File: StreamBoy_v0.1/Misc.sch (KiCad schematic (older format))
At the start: 3 parts, among them IC1 LY68L6400SLIT, J2 USB_B_Micro, U4 CP2102N-A01-GQFN24

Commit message: Bunch of stuff
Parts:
- added C10, C5, C6, C7, C8, C9, C? (x2): C, Capacitor_SMD:C_0805_2012Metric, symbol Device:C
- added J?: TF-015, TF015, symbol TF-015:TF-015
- added Q1, Q2: SS8050-G, SOT95P240X115-3N, symbol SS8050-G:SS8050-G
- added R47, R48, R49, R50, R51: R, Resistor_SMD:R_0805_2012Metric, symbol Device:R
- added X?: SG-7050CBN, Oscillator:Oscillator_SMD_SeikoEpson_SG8002CA-4Pin_7.0x5.0mm, symbol Oscillator:SG-7050CBN
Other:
- moved on the sheet: IC1

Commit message: Power to the masses
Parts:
- removed C?: C, Capacitor_SMD:C_0805_2012Metric, symbol Device:C
- added C2: 15pF, Capacitor_SMD:C_0805_2012Metric, symbol Device:C
- C1: renamed from C?; value C -> 0.1uF
- gave numbers to parts that had none: 1
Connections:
- net labels added: FPGA_CLK_50M, GND, USB5V
- wire segments 8 -> 14
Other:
- moved on the sheet: C1, X1
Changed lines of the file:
@@
 $EndComp
 $Comp
-L Oscillator:SG-7050CBN X?
+L Oscillator:SG-7050CBN X1
 U 1 1 5E0DA99D
-P 8150 4850
-F 0 "X?" H 8494 4896 50  0000 L CNN
-F 1 "SG-7050CBN" H 8494 4805 50  0000 L CNN
-F 2 "Oscillator:Oscillator_SMD_SeikoEpson_SG8002CA-4Pin_7.0x5.0mm" H 8850 4500 50  0001 C CNN
-F 3 "https://support.epson.biz/td/api/doc_check.php?dl=brief_SG7050CBN&lang=en" H 8050 4850 50  0001 C CNN
-	1    8150 4850
+P 9850 5750
+F 0 "X1" H 10000 5500 50  0000 L CNN
+F 1 "SG-7050CBN" H 10000 5400 50  0000 L CNN
+F 2 "Oscillator:Oscillator_SMD_SeikoEpson_SG8002CA-4Pin_7.0x5.0mm" H 10550 5400 50  0001 C CNN
+F 3 "https://support.epson.biz/td/api/doc_check.php?dl=brief_SG7050CBN&lang=en" H 9750 5750 50  0001 C CNN
+	1    9850 5750
 	1    0    0    -1
 $EndComp
@@
 L Device:C C?
 U 1 1 5E0DB62B
-P 9450 4900
+P 9850 5150
 AR Path="/5E0FF68C/5E0DB62B" Ref="C?"  Part="1"
-AR Path="/5E07E0B7/5E0DB62B" Ref="C?"  Part="1"
-F 0 "C?" H 9565 4946 50  0000 L CNN
-F 1 "C" H 9565 4855 50  0000 L CNN
-F 2 "Capacitor_SMD:C_0805_2012Metric" H 9488 4750 50  0001 C CNN
-F 3 "~" H 9450 4900 50  0001 C CNN
-	1    9450 4900
+AR Path="/5E07E0B7/5E0DB62B" Ref="C1"  Part="1"
+F 0 "C1" H 9965 5196 50  0000 L CNN
+F 1 "0.1uF" H 9965 5105 50  0000 L CNN
+F 2 "Capacitor_SMD:C_0805_2012Metric" H 9888 5000 50  0001 C CNN
+F 3 "https://datasheet.lcsc.com/szlcsc/1912111437_Shenzhen-SCTF-Elec-S7D50-000000A20F30T_C387131.pdf" H 9850 5150 50  0001 C CNN
+	1    9850 5150
 	1    0    0    -1
 $EndComp
 $Comp
 L Device:C C?
-U 1 1 5E0DB631
-P 9800 4900
-AR Path="/5E0FF68C/5E0DB631" Ref="C?"  Part="1"
-AR Path="/5E07E0B7/5E0DB631" Ref="C?"  Part="1"
-F 0 "C?" H 9915 4946 50  0000 L CNN
-F 1 "C" H 9915 4855 50  0000 L CNN
-F 2 "Capacitor_SMD:C_0805_2012Metric" H 9838 4750 50  0001 C CNN
-F 3 "~" H 9800 4900 50  0001 C CNN
-	1    9800 4900
+U 1 1 5E0F5C50
+P 10450 5750
+AR Path="/5E0FF68C/5E0F5C50" Ref="C?"  Part="1"
+AR Path="/5E07E0B7/5E0F5C50" Ref="C2"  Part="1"
+F 0 "C2" H 10565 5796 50  0000 L CNN
+F 1 "15pF" H 10565 5705 50  0000 L CNN
+F 2 "Capacitor_SMD:C_0805_2012Metric" H 10488 5600 50  0001 C CNN
+F 3 "https://datasheet.lcsc.com/szlcsc/1912111437_Shenzhen-SCTF-Elec-S7D50-000000A20F30T_C387131.pdf" H 10450 5750 50  0001 C CNN
+	1    10450 5750
+	0    -1   -1   0
+$EndComp
+Text GLabel 9850 5000 1    50   Input ~ 0
+VCC3
+Wire Wire Line
+	10150 5750 10300 5750
+Wire Wire Line
+	10300 5750 10300 5450
+Connection ~ 10300 5750
+Text GLabel 10300 5450 1    50   Input ~ 0
+FPGA_CLK_50M
+$Comp
+L power:GND #PWR?
+U 1 1 5E0FED92
+P 10600 5750
+F 0 "#PWR?" H 10600 5500 50  0001 C CNN
+F 1 "GND" V 10605 5622 50  0000 R CNN
+F 2 "" H 10600 5750 50  0001 C CNN
+F 3 "" H 10600 5750 50  0001 C CNN
+	1    10600 5750
+	0    -1   -1   0
+$EndComp
+Wire Wire Line
+	9850 5300 9850 5450
+Wire Wire Line
+	9850 5450 9550 5450
+Wire Wire Line
+	9550 5450 9550 5750
+Connection ~ 9850 5450
+$Comp
+L power:GND #PWR?
+U 1 1 5E100DF1
+P 9850 6050
+F 0 "#PWR?" H 9850 5800 50  0001 C CNN
+F 1 "GND" H 9855 5877 50  0000 C CNN
+F 2 "" H 9850 6050 50  0001 C CNN
+F 3 "" H 9850 6050 50  0001 C CNN
+	1    9850 6050
 	1    0    0    -1
 $EndComp
+Wire Wire Line
+	3250 4300 3100 4300
+Text GLabel 3250 4300 2    50   Input ~ 0
+USB5V
 $EndSCHEMATC

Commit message: Connect uart
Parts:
- removed C10, C5, C6, C7, C8, C9: C, Capacitor_SMD:C_0805_2012Metric, symbol Device:C
- removed J?: TF-015, TF015, symbol TF-015:TF-015
- removed Q1, Q2: SS8050-G, SOT95P240X115-3N, symbol SS8050-G:SS8050-G
- removed R47, R48, R49, R50, R51: R, Resistor_SMD:R_0805_2012Metric, symbol Device:R
- removed U4: CP2102N-A01-GQFN24, Package_DFN_QFN:QFN-24-1EP_4x4mm_P0.5mm_EP2.6x2.6mm, symbol Interface_USB:CP2102N-A01-GQFN24
- added C? (x2): 0.1uF, Capacitor_SMD:C_0805_2012Metric, symbol Device:C
- added C?: 1uF, Capacitor_SMD:C_0805_2012Metric, symbol Device:C
- added C?: 4.7uF, Capacitor_SMD:C_0805_2012Metric, symbol Device:C
- added Q? (x2): SS8050-G, SOT95P240X115-3N, symbol SS8050-G:SS8050-G
- added R? (x3): 10K, Resistor_SMD:R_0805_2012Metric, symbol Device:R
- added R?: 2K, Resistor_SMD:R_0805_2012Metric, symbol Device:R
- added UUART: CP2102N-A01-GQFN28, Package_DFN_QFN:QFN-28-1EP_5x5mm_P0.5mm_EP3.35x3.35mm, symbol Interface_USB:CP2102N-A01-GQFN28
- renumbered J2 to JUSB
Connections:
- net labels added: ESP_DTR, ESP_EN, ESP_IO0, ESP_RTS, ESP_RX, ESP_TX
- wire segments 14 -> 59
- no-connect marks 0 -> 16
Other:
- moved on the sheet: IC1, JUSB

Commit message: Flip RX/TX, Move esp prog. circuit
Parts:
- removed Q? (x2): SS8050-G, SOT95P240X115-3N, symbol SS8050-G:SS8050-G
- removed R? (x2): 10K, Resistor_SMD:R_0805_2012Metric, symbol Device:R
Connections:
- net labels removed: ESP_EN, ESP_IO0
- wire segments 59 -> 45
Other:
- note added: "Note, RX/TX are flipped"
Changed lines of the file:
@@
 	0    -1   -1   0
-$EndComp
-$Comp
-L Device:R R?
-U 1 1 5E0BF601
-P 8700 1650
-AR Path="/5E0FF68C/5E0BF601" Ref="R?"  Part="1"
-AR Path="/5E07E0B7/5E0BF601" Ref="R?"  Part="1"
-F 0 "R?" H 8770 1696 50  0000 L CNN
-F 1 "10K" H 8770 1605 50  0000 L CNN
-F 2 "Resistor_SMD:R_0805_2012Metric" V 8630 1650 50  0001 C CNN
-F 3 "~" H 8700 1650 50  0001 C CNN
-	1    8700 1650
-	0    1    1    0
-$EndComp
-$Comp
-L Device:R R?
-U 1 1 5E0BFA7F
-P 8700 2400
-AR Path="/5E0FF68C/5E0BFA7F" Ref="R?"  Part="1"
-AR Path="/5E07E0B7/5E0BFA7F" Ref="R?"  Part="1"
-F 0 "R?" H 8770 2446 50  0000 L CNN
-F 1 "10K" H 8770 2355 50  0000 L CNN
-F 2 "Resistor_SMD:R_0805_2012Metric" V 8630 2400 50  0001 C CNN
-F 3 "~" H 8700 2400 50  0001 C CNN
-	1    8700 2400
-	0    1    1    0
-$EndComp
-$Comp
-L SS8050-G:SS8050-G Q?
-U 1 1 5E0BFFFE
-P 9100 1650
-F 0 "Q?" H 9638 1696 50  0000 L CNN
-F 1 "SS8050-G" H 9638 1605 50  0000 L CNN
-F 2 "SOT95P240X115-3N" H 9100 1650 50  0001 L BNN
-F 3 "1.15mm" H 9100 1650 50  0001 L BNN
-F 4 "Bipolar Transistors - BJT NPN TRANSISTOR 1.5A 40V" H 9100 1650 50  0001 L BNN "Field4"
-F 5 "Comchip Technology" H 9100 1650 50  0001 L BNN "Field5"
-F 6 "" H 9100 1650 50  0001 L BNN "Field6"
-F 7 "" H 9100 1650 50  0001 L BNN "Field7"
-F 8 "SS8050-G" H 9100 1650 50  0001 L BNN "Field8"
-	1    9100 1650
-	1    0    0    -1
-$EndComp
-$Comp
-L SS8050-G:SS8050-G Q?
-U 1 1 5E0C0B15
-P 9100 2400
-F 0 "Q?" H 9638 2446 50  0000 L CNN
-F 1 "SS8050-G" H 9638 2355 50  0000 L CNN
-F 2 "SOT95P240X115-3N" H 9100 2400 50  0001 L BNN
-F 3 "1.15mm" H 9100 2400 50  0001 L BNN
-F 4 "Bipolar Transistors - BJT NPN TRANSISTOR 1.5A 40V" H 9100 2400 50  0001 L BNN "Field4"
-F 5 "Comchip Technology" H 9100 2400 50  0001 L BNN "Field5"
-F 6 "" H 9100 2400 50  0001 L BNN "Field6"
-F 7 "" H 9100 2400 50  0001 L BNN "Field7"
-F 8 "SS8050-G" H 9100 2400 50  0001 L BNN "Field8"
-	1    9100 2400
-	1    0    0    1
 $EndComp
 Text GLabel 3800 1850 2    50   Input ~ 0
 ESP_RTS
+Text GLabel 3800 2050 2    50   Input ~ 0
+ESP_RX
 Text GLabel 3800 1950 2    50   Input ~ 0
-ESP_RX
-Text GLabel 3800 2050 2    50   Input ~ 0
 ESP_TX
 Text GLabel 3800 2250 2    50   Input ~ 0
 ESP_DTR
-Text GLabel 8250 1650 0    50   Input ~ 0
-ESP_DTR
-Text GLabel 8250 2400 0    50   Input ~ 0
-ESP_RTS
-Wire Wire Line
-	8250 1650 8450 1650
-Wire Wire Line
-	8550 2400 8500 2400
-Wire Wire Line
-	9100 2400 8850 2400
-Wire Wire Line
-	8850 1650 9100 1650
-Text GLabel 10300 1250 2    50   Input ~ 0
-ESP_EN
-Text GLabel 10300 2800 2    50   Input ~ 0
-ESP_IO0
-Wire Wire Line
-	10300 1250 9500 1250
-Wire Wire Line
-	9500 1250 9500 1350
-Wire Wire Line
-	10300 2800 9500 2800
-Wire Wire Line
-	9500 2800 9500 2700
-Wire Wire Line
-	9500 1950 8500 1950
-Wire Wire Line
-	8500 1950 8500 2400
-Connection ~ 8500 2400
-Wire Wire Line
-	8500 2400 8250 2400
-Wire Wire Line
-	9500 2100 8450 2100
-Wire Wire Line
-	8450 2100 8450 1650
-Connection ~ 8450 1650
-Wire Wire Line
-	8450 1650 8550 1650
 Text GLabel 2100 1950 0    50   Input ~ 0
 VCC3
@@
 Wire Wire Line
 	1950 2350 2650 2350
+Text Notes 4150 2000 0    50   ~ 0
+Note, RX/TX are flipped
 $EndSCHEMATC

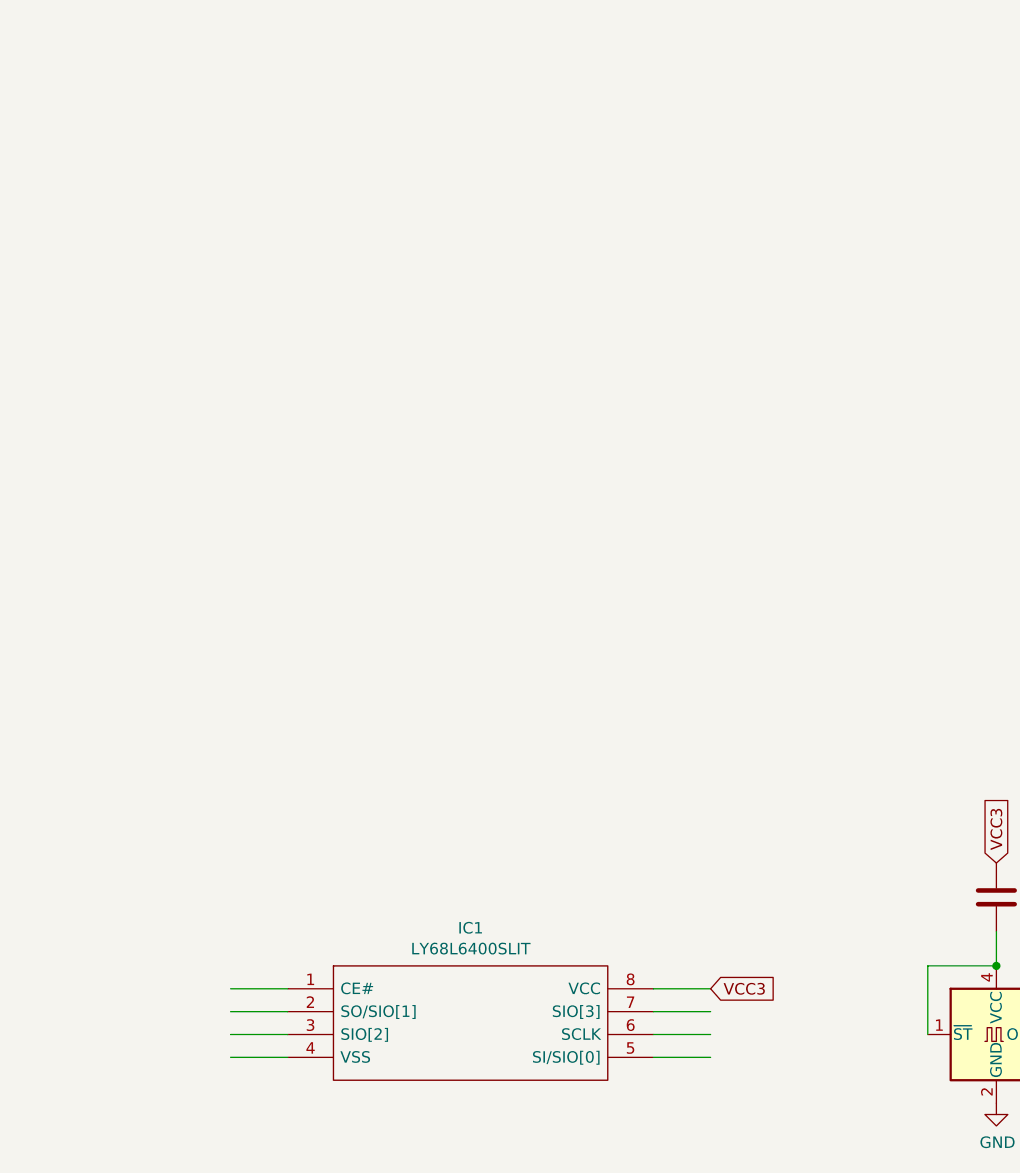
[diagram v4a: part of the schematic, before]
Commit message: Connect RAM temporarily
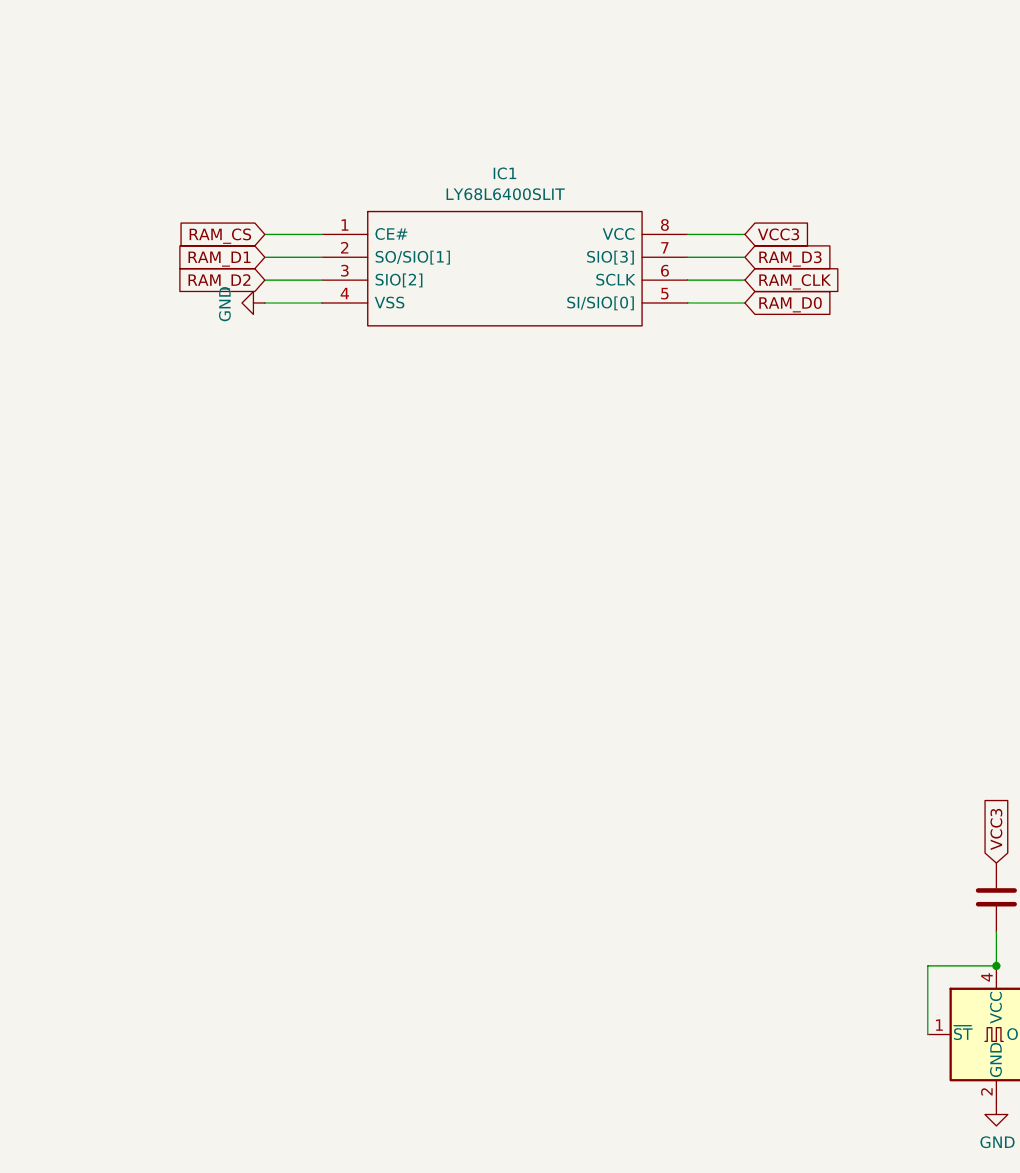
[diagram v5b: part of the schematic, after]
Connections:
- net labels added: RAM_CLK, RAM_CS, RAM_D0, RAM_D1, RAM_D2, RAM_D3
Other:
- moved on the sheet: IC1
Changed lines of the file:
@@
 $EndDescr
-$Comp
-L LY68L6400SLIT:LY68L6400SLIT IC1
-U 1 1 5E092BFD
-P 6750 5550
-F 0 "IC1" H 7550 5815 50  0000 C CNN
-F 1 "LY68L6400SLIT" H 7550 5724 50  0000 C CNN
-F 2 "SOIC127P600X175-8N" H 8200 5650 50  0001 L CNN
-F 3 "https://datasheet.lcsc.com/szlcsc/Lyontek-Inc-LY68L6400SLIT_C261881.pdf" H 8200 5550 50  0001 L CNN
-F 4 "AM SRAM 64Mb (8M x 8) SPI/ QPI SOP-8_150mil RoHS" H 8200 5450 50  0001 L CNN "Description"
-F 5 "1.75" H 8200 5350 50  0001 L CNN "Height"
-F 6 "Lyontek Inc." H 8200 5250 50  0001 L CNN "Manufacturer_Name"
-F 7 "LY68L6400SLIT" H 8200 5150 50  0001 L CNN "Manufacturer_Part_Number"
-F 8 "" H 8200 5050 50  0001 L CNN "Mouser Part Number"
-F 9 "" H 8200 4950 50  0001 L CNN "Mouser Price/Stock"
-F 10 "" H 8200 4850 50  0001 L CNN "RS Part Number"
-F 11 "" H 8200 4750 50  0001 L CNN "RS Price/Stock"
-	1    6750 5550
-	1    0    0    -1
-$EndComp
-Wire Wire Line
-	6750 5550 6500 5550
-Wire Wire Line
-	6750 5650 6500 5650
-Wire Wire Line
-	6750 5750 6500 5750
-Wire Wire Line
-	6750 5850 6500 5850
-Wire Wire Line
-	8350 5850 8600 5850
-Wire Wire Line
-	8350 5750 8600 5750
-Wire Wire Line
-	8350 5650 8600 5650
-Wire Wire Line
-	8350 5550 8600 5550
-Text GLabel 8600 5550 2    50   Input ~ 0
-VCC3
 $Comp
 L Oscillator:SG-7050CBN X1
@@
 Text Notes 4150 2000 0    50   ~ 0
 Note, RX/TX are flipped
+Text GLabel 8750 2250 2    50   Input ~ 0
+VCC3
+Wire Wire Line
+	8500 2250 8750 2250
+Wire Wire Line
+	8500 2350 8750 2350
+Wire Wire Line
+	8500 2450 8750 2450
+Wire Wire Line
+	8500 2550 8750 2550
+Wire Wire Line
+	6900 2550 6650 2550
+Wire Wire Line
+	6900 2450 6650 2450
+Wire Wire Line
+	6900 2350 6650 2350
+Wire Wire Line
+	6900 2250 6650 2250
+$Comp
+L LY68L6400SLIT:LY68L6400SLIT IC1
+U 1 1 5E092BFD
+P 6900 2250
+F 0 "IC1" H 7700 2515 50  0000 C CNN
+F 1 "LY68L6400SLIT" H 7700 2424 50  0000 C CNN
+F 2 "SOIC127P600X175-8N" H 8350 2350 50  0001 L CNN
+F 3 "https://datasheet.lcsc.com/szlcsc/Lyontek-Inc-LY68L6400SLIT_C261881.pdf" H 8350 2250 50  0001 L CNN
+F 4 "AM SRAM 64Mb (8M x 8) SPI/ QPI SOP-8_150mil RoHS" H 8350 2150 50  0001 L CNN "Description"
+F 5 "1.75" H 8350 2050 50  0001 L CNN "Height"
+F 6 "Lyontek Inc." H 8350 1950 50  0001 L CNN "Manufacturer_Name"
+F 7 "LY68L6400SLIT" H 8350 1850 50  0001 L CNN "Manufacturer_Part_Number"
+F 8 "" H 8350 1750 50  0001 L CNN "Mouser Part Number"
+F 9 "" H 8350 1650 50  0001 L CNN "Mouser Price/Stock"
+F 10 "" H 8350 1550 50  0001 L CNN "RS Part Number"
+F 11 "" H 8350 1450 50  0001 L CNN "RS Price/Stock"
+	1    6900 2250
+	1    0    0    -1
+$EndComp
+Text GLabel 8750 2450 2    50   Input ~ 0
+RAM_CLK
+Text GLabel 8750 2550 2    50   Input ~ 0
+RAM_D0
+Text GLabel 8750 2350 2    50   Input ~ 0
+RAM_D3
+Text GLabel 6650 2450 0    50   Input ~ 0
+RAM_D2
+Text GLabel 6650 2350 0    50   Input ~ 0
+RAM_D1
+Text GLabel 6650 2250 0    50   Input ~ 0
+RAM_CS
+$Comp
+L power:GND #PWR?
+U 1 1 5E179831
+P 6650 2550
+F 0 "#PWR?" H 6650 2300 50  0001 C CNN
+F 1 "GND" H 6655 2377 50  0000 C CNN
+F 2 "" H 6650 2550 50  0001 C CNN
+F 3 "" H 6650 2550 50  0001 C CNN
+	1    6650 2550
+	0    1    1    0
+$EndComp
 $EndSCHEMATC

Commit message: Update some labels
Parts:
- gave numbers to parts that had none: 6
- renumbered JUSB to JUSB1, UUART to U12
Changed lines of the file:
@@
 $EndComp
 $Comp
-L power:GND #PWR?
+L power:GND #PWR0125
 U 1 1 5E0AE37F
 P 1000 2900
-F 0 "#PWR?" H 1000 2650 50  0001 C CNN
+F 0 "#PWR0125" H 1000 2650 50  0001 C CNN
 F 1 "GND" H 1005 2727 50  0000 C CNN
 F 2 "" H 1000 2900 50  0001 C CNN
@@
 P 3900 2650
 AR Path="/5E0FF68C/5E0B4B8D" Ref="R?"  Part="1"
-AR Path="/5E07E0B7/5E0B4B8D" Ref="R?"  Part="1"
-F 0 "R?" H 3970 2696 50  0000 L CNN
+AR Path="/5E07E0B7/5E0B4B8D" Ref="R12"  Part="1"
+F 0 "R12" H 3970 2696 50  0000 L CNN
 F 1 "10K" H 3970 2605 50  0000 L CNN
 F 2 "Resistor_SMD:R_0805_2012Metric" V 3830 2650 50  0001 C CNN
@@
 $EndComp
 $Comp
-L power:GND #PWR?
+L power:GND #PWR0126
 U 1 1 5E0B51BC
 P 4200 2650
-F 0 "#PWR?" H 4200 2400 50  0001 C CNN
+F 0 "#PWR0126" H 4200 2400 50  0001 C CNN
 F 1 "GND" H 4205 2477 50  0000 C CNN
 F 2 "" H 4200 2650 50  0001 C CNN
@@
 P 2400 1950
 AR Path="/5E0FF68C/5E0D0203" Ref="R?"  Part="1"
-AR Path="/5E07E0B7/5E0D0203" Ref="R?"  Part="1"
-F 0 "R?" H 2470 1996 50  0000 L CNN
+AR Path="/5E07E0B7/5E0D0203" Ref="R11"  Part="1"
+F 0 "R11" H 2470 1996 50  0000 L CNN
 F 1 "2K" H 2470 1905 50  0000 L CNN
 F 2 "Resistor_SMD:R_0805_2012Metric" V 2330 1950 50  0001 C CNN
@@
 P 2700 1200
 AR Path="/5E0FF68C/5E0DC6A6" Ref="C?"  Part="1"
-AR Path="/5E07E0B7/5E0DC6A6" Ref="C?"  Part="1"
-F 0 "C?" H 2815 1246 50  0000 L CNN
+AR Path="/5E07E0B7/5E0DC6A6" Ref="C8"  Part="1"
+F 0 "C8" H 2815 1246 50  0000 L CNN
 F 1 "0.1uF" H 2815 1155 50  0000 L CNN
 F 2 "Capacitor_SMD:C_0805_2012Metric" H 2738 1050 50  0001 C CNN
@@
 P 2200 1200
 AR Path="/5E0FF68C/5E0DDFA3" Ref="C?"  Part="1"
-AR Path="/5E07E0B7/5E0DDFA3" Ref="C?"  Part="1"
-F 0 "C?" H 2315 1246 50  0000 L CNN
+AR Path="/5E07E0B7/5E0DDFA3" Ref="C7"  Part="1"
+F 0 "C7" H 2315 1246 50  0000 L CNN
 F 1 "1uF" H 2315 1155 50  0000 L CNN
 F 2 "Capacitor_SMD:C_0805_2012Metric" H 2238 1050 50  0001 C CNN
@@
 $EndComp
 $Comp
-L power:GND #PWR?
+L power:GND #PWR0127
 U 1 1 5E0DE66B
 P 2200 900
-F 0 "#PWR?" H 2200 650 50  0001 C CNN
+F 0 "#PWR0127" H 2200 650 50  0001 C CNN
 F 1 "GND" H 2205 727 50  0000 C CNN
 F 2 "" H 2200 900 50  0001 C CNN
@@
 VCC3
 $Comp
-L Interface_USB:CP2102N-A01-GQFN28 UUART
+L Interface_USB:CP2102N-A01-GQFN28 U12
 U 1 1 5E0E977D
 P 3150 2850
-F 0 "UUART" H 3150 1461 50  0000 C CNN
+F 0 "U12" H 3150 1461 50  0000 C CNN
 F 1 "CP2102N-A01-GQFN28" H 3150 1370 50  0000 C CNN
 F 2 "Package_DFN_QFN:QFN-28-1EP_5x5mm_P0.5mm_EP3.35x3.35mm" H 3600 1650 50  0001 L CNN
@@
 P 4000 1200
 AR Path="/5E0FF68C/5E102D99" Ref="C?"  Part="1"
-AR Path="/5E07E0B7/5E102D99" Ref="C?"  Part="1"
-F 0 "C?" H 4115 1246 50  0000 L CNN
+AR Path="/5E07E0B7/5E102D99" Ref="C10"  Part="1"
+F 0 "C10" H 4115 1246 50  0000 L CNN
 F 1 "0.1uF" H 4115 1155 50  0000 L CNN
 F 2 "Capacitor_SMD:C_0805_2012Metric" H 4038 1050 50  0001 C CNN
@@
 P 3500 1200
 AR Path="/5E0FF68C/5E102D9F" Ref="C?"  Part="1"
-AR Path="/5E07E0B7/5E102D9F" Ref="C?"  Part="1"
-F 0 "C?" H 3615 1246 50  0000 L CNN
+AR Path="/5E07E0B7/5E102D9F" Ref="C9"  Part="1"
+F 0 "C9" H 3615 1246 50  0000 L CNN
 F 1 "4.7uF" H 3615 1155 50  0000 L CNN
 F 2 "Capacitor_SMD:C_0805_2012Metric" H 3538 1050 50  0001 C CNN
@@
 $EndComp
 $Comp
-L power:GND #PWR?
+L power:GND #PWR0128
 U 1 1 5E102DA5
 P 3500 900
-F 0 "#PWR?" H 3500 650 50  0001 C CNN
+F 0 "#PWR0128" H 3500 650 50  0001 C CNN
 F 1 "GND" H 3505 727 50  0000 C CNN
 F 2 "" H 3500 900 50  0001 C CNN
@@
 NoConn ~ 3650 3950
 $Comp
-L power:GND #PWR?
+L power:GND #PWR0129
 U 1 1 5E12E83F
 P 3150 4400
-F 0 "#PWR?" H 3150 4150 50  0001 C CNN
+F 0 "#PWR0129" H 3150 4150 50  0001 C CNN
 F 1 "GND" H 3155 4227 50  0000 C CNN
 F 2 "" H 3150 4400 50  0001 C CNN
@@
 NoConn ~ 1400 2550
 $Comp
-L Connector:USB_B_Micro JUSB
+L Connector:USB_B_Micro JUSB1
 U 1 1 5E07FC2B
 P 1100 2350
-F 0 "JUSB" H 1157 2817 50  0000 C CNN
+F 0 "JUSB1" H 1157 2817 50  0000 C CNN
 F 1 "USB_B_Micro" H 1157 2726 50  0000 C CNN
 F 2 "Connector_USB:USB_Micro-B_Molex_47346-0001" H 1250 2300 50  0001 C CNN
@@
 RAM_CS
 $Comp
-L power:GND #PWR?
+L power:GND #PWR0130
 U 1 1 5E179831
 P 6650 2550
-F 0 "#PWR?" H 6650 2300 50  0001 C CNN
+F 0 "#PWR0130" H 6650 2300 50  0001 C CNN
 F 1 "GND" H 6655 2377 50  0000 C CNN
 F 2 "" H 6650 2550 50  0001 C CNN

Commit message: I hate component placement!
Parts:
- C1, C2, C9: footprint Capacitor_SMD:C_0805_2012Metric -> Capacitor_SMD:C_0402_1005Metric
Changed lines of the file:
@@
 EESchema Schematic File Version 4
-LIBS:StreamBoy-cache
-EELAYER 29 0
+EELAYER 30 0
 EELAYER END
 $Descr A4 11693 8268
@@
 F 0 "C1" H 9965 5196 50  0000 L CNN
 F 1 "0.1uF" H 9965 5105 50  0000 L CNN
-F 2 "Capacitor_SMD:C_0805_2012Metric" H 9888 5000 50  0001 C CNN
+F 2 "Capacitor_SMD:C_0402_1005Metric" H 9888 5000 50  0001 C CNN
 F 3 "https://datasheet.lcsc.com/szlcsc/1912111437_Shenzhen-SCTF-Elec-S7D50-000000A20F30T_C387131.pdf" H 9850 5150 50  0001 C CNN
 	1    9850 5150
@@
 F 0 "C2" H 10565 5796 50  0000 L CNN
 F 1 "15pF" H 10565 5705 50  0000 L CNN
-F 2 "Capacitor_SMD:C_0805_2012Metric" H 10488 5600 50  0001 C CNN
+F 2 "Capacitor_SMD:C_0402_1005Metric" H 10488 5600 50  0001 C CNN
 F 3 "https://datasheet.lcsc.com/szlcsc/1912111437_Shenzhen-SCTF-Elec-S7D50-000000A20F30T_C387131.pdf" H 10450 5750 50  0001 C CNN
 	1    10450 5750
@@
 F 0 "C9" H 3615 1246 50  0000 L CNN
 F 1 "4.7uF" H 3615 1155 50  0000 L CNN
-F 2 "Capacitor_SMD:C_0805_2012Metric" H 3538 1050 50  0001 C CNN
+F 2 "Capacitor_SMD:C_0402_1005Metric" H 3538 1050 50  0001 C CNN
 F 3 "~" H 3500 1200 50  0001 C CNN
 	1    3500 1200
